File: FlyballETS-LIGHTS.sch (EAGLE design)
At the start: 21 parts, among them IC1 74HC595N, IC2 ULN2003AN, IC3 LM555N

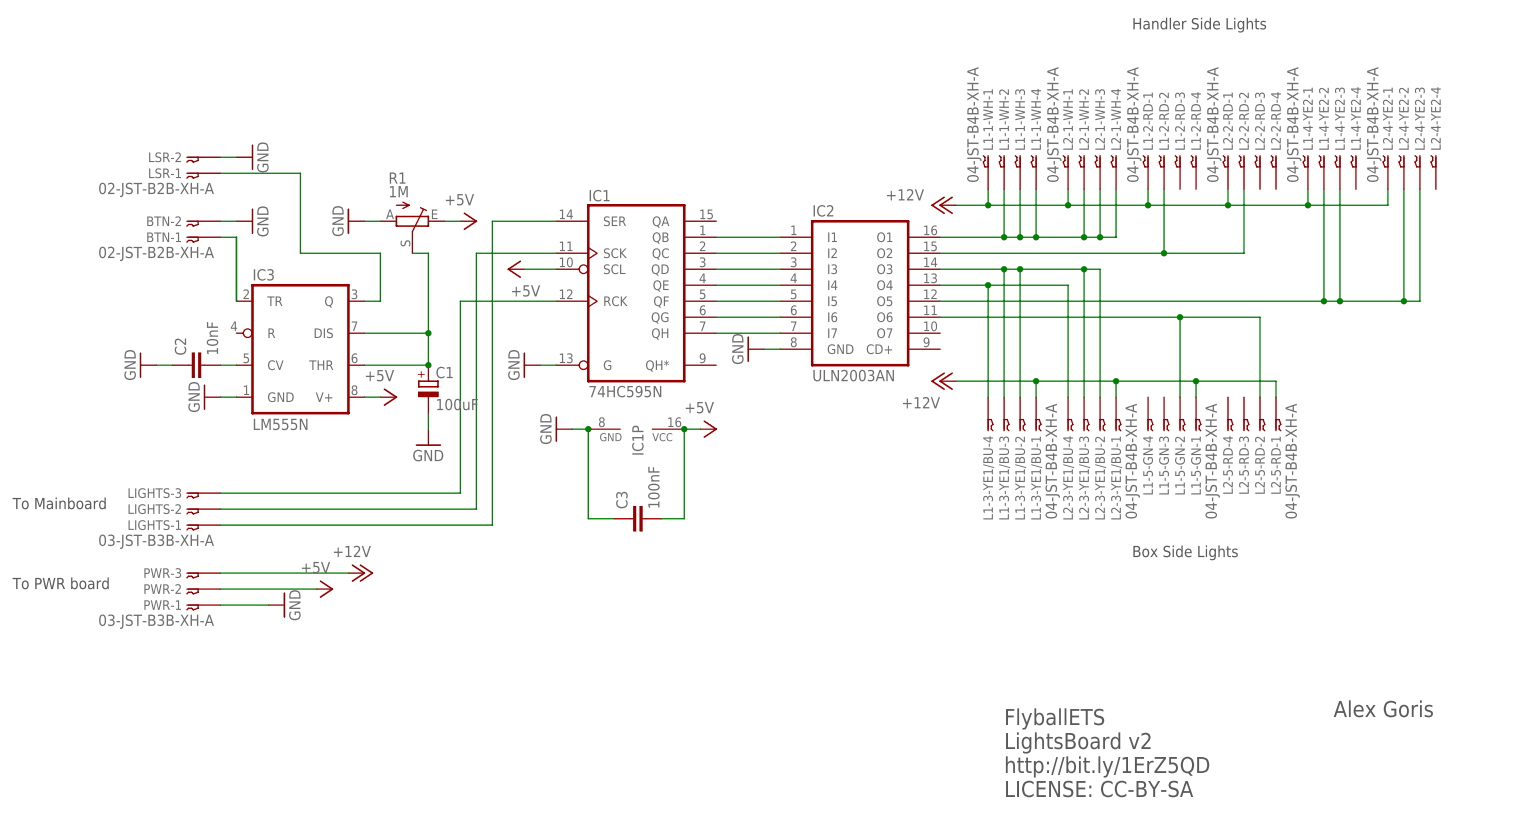
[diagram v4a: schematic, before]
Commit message: Fixed JST XH pin numbering
Updated bt_con-jst-xh.lbr library with swapped pin numbering.
Updated all board designs with updated library so they have the
connectors the right way around
Fixes #4
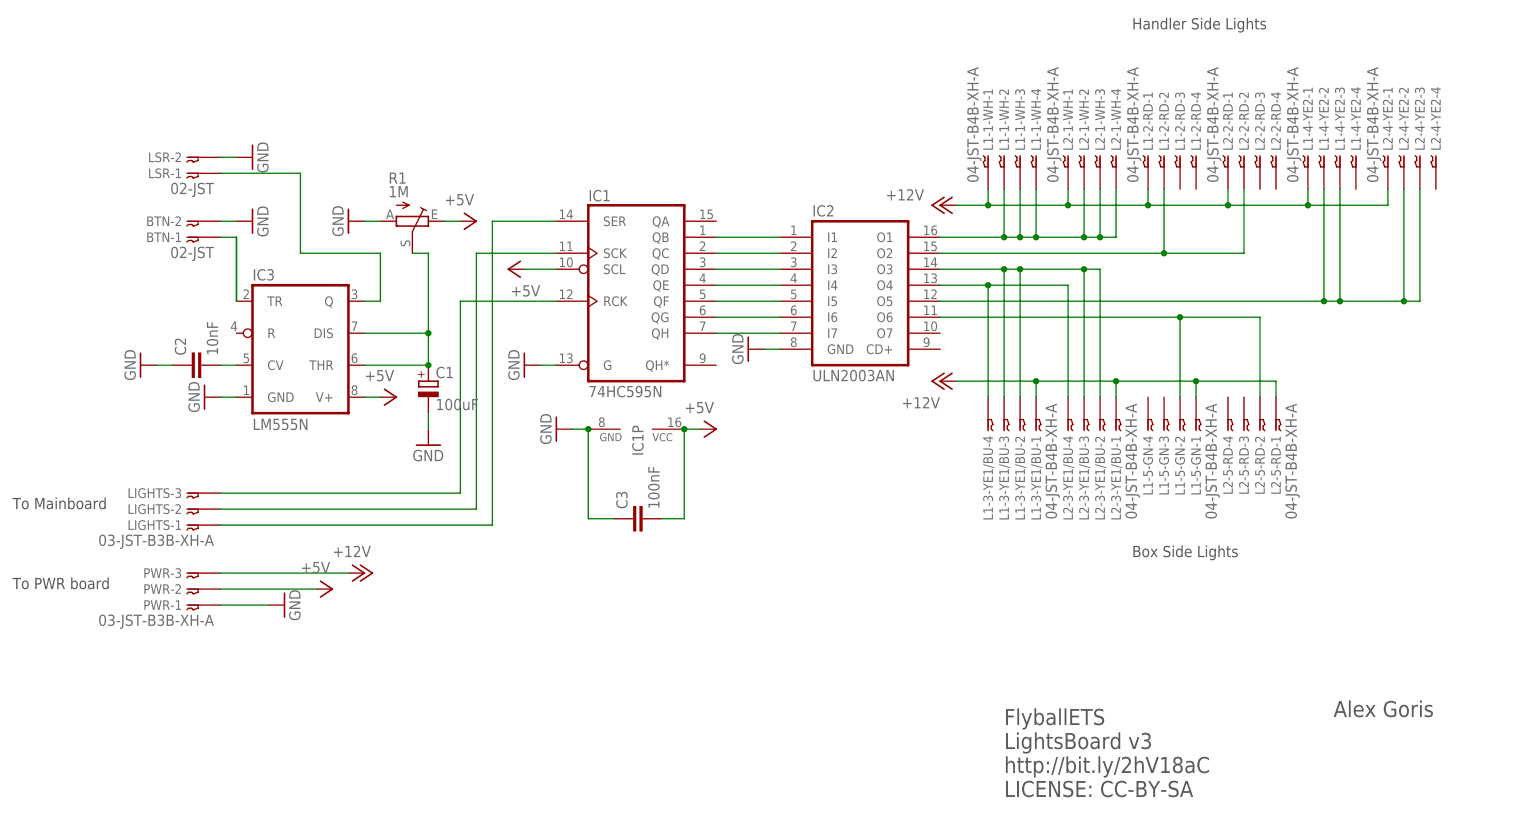
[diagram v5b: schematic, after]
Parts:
- BTN, LSR: value 02-JST-B2B-XH-A -> 02-JST; device bt_con-jst-xh:02-JST-B2B-XH-A -> bt_con-jst-xh:02-JST
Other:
- note added: "FlyballETS LightsBoard v3 http://bit.ly/2hV18aC LICENSE: CC-BY-SA"
- note removed: "FlyballETS LightsBoard v2 http://bit.ly/1ErZ5QD LICENSE: CC-BY-SA"
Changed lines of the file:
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@@
 <?xml version="1.0" encoding="utf-8"?>
 <!DOCTYPE eagle SYSTEM "eagle.dtd">
-<eagle version="7.5.0">
+<eagle version="8.2.2">
 <drawing>
 <settings>
@@
 </classes>
 <parts>
-<part name="BTN" library="bt_con-jst-xh" deviceset="02-JST" device="-B2B-XH-A"/>
-<part name="IC1" library="74xx-eu" deviceset="74*595" device="N" technology="HC"/>
-<part name="IC2" library="uln-udn" deviceset="ULN2003A" device="N"/>
-<part name="IC3" library="linear" deviceset="*555" device="N" technology="LM"/>
-<part name="R1" library="pot" deviceset="TRIM_EU-" device="B25P" value="1M"/>
-<part name="C1" library="resistor" deviceset="CPOL-EU" device="E2.5-7" value="100uF"/>
+<part name="BTN" library="bt_con-jst-xh" deviceset="02-JST" device=""/>
+<part name="IC1" library="74xx-eu" library_urn="urn:adsk.eagle:library:85" deviceset="74*595" device="N" technology="HC"/>
+<part name="IC2" library="uln-udn" library_urn="urn:adsk.eagle:library:407" deviceset="ULN2003A" device="N"/>
+<part name="IC3" library="linear" library_urn="urn:adsk.eagle:library:262" deviceset="*555" device="N" technology="LM"/>
+<part name="R1" library="pot" library_urn="urn:adsk.eagle:library:331" deviceset="TRIM_EU-" device="B25P" value="1M"/>
+<part name="C1" library="resistor" library_urn="urn:adsk.eagle:library:348" deviceset="CPOL-EU" device="E2.5-7" value="100uF"/>
 <part name="PWR" library="bt_con-jst-xh" deviceset="03-JST" device="-B3B-XH-A"/>
-<part name="GND1" library="supply1" deviceset="GND" device=""/>
-<part name="P+1" library="supply1" deviceset="+5V" device=""/>
-<part name="P+2" library="supply1" deviceset="+12V" device=""/>
+<part name="GND1" library="supply1" library_urn="urn:adsk.eagle:library:371" deviceset="GND" device=""/>
+<part name="P+1" library="supply1" library_urn="urn:adsk.eagle:library:371" deviceset="+5V" device=""/>
+<part name="P+2" library="supply1" library_urn="urn:adsk.eagle:library:371" deviceset="+12V" device=""/>
 <part name="LIGHTS" library="bt_con-jst-xh" deviceset="03-JST" device="-B3B-XH-A"/>
-<part name="P+3" library="supply1" deviceset="+5V" device=""/>
-<part name="GND2" library="supply1" deviceset="GND" device=""/>
-<part name="GND3" library="supply1" deviceset="GND" device=""/>
-<part name="GND4" library="supply1" deviceset="GND" device=""/>
+<part name="P+3" library="supply1" library_urn="urn:adsk.eagle:library:371" deviceset="+5V" device=""/>
+<part name="GND2" library="supply1" library_urn="urn:adsk.eagle:library:371" deviceset="GND" device=""/>
+<part name="GND3" library="supply1" library_urn="urn:adsk.eagle:library:371" deviceset="GND" device=""/>
+<part name="GND4" library="supply1" library_urn="urn:adsk.eagle:library:371" deviceset="GND" device=""/>
 <part name="L2-5-RD" library="bt_con-jst-xh" deviceset="04-JST" device="-B4B-XH-A"/>
 <part name="L2-4-YE2" library="bt_con-jst-xh" deviceset="04-JST" device="-B4B-XH-A"/>
@@
 <part name="L1-4-YE2" library="bt_con-jst-xh" deviceset="04-JST" device="-B4B-XH-A"/>
 <part name="L1-5-GN" library="bt_con-jst-xh" deviceset="04-JST" device="-B4B-XH-A"/>
-<part name="P+4" library="supply1" deviceset="+12V" device=""/>
-<part name="P+9" library="supply1" deviceset="+5V" device=""/>
-<part name="GND5" library="supply1" deviceset="GND" device=""/>
-<part name="P+10" library="supply1" deviceset="+5V" device=""/>
-<part name="GND6" library="supply1" deviceset="GND" device=""/>
-<part name="GND7" library="supply1" deviceset="GND" device=""/>
-<part name="C2" library="resistor" deviceset="C-EU" device="050-030X075" value="10nF"/>
-<part name="GND8" library="supply1" deviceset="GND" device=""/>
-<part name="GND9" library="supply1" deviceset="GND" device=""/>
-<part name="LSR" library="bt_con-jst-xh" deviceset="02-JST" device="-B2B-XH-A"/>
-<part name="GND10" library="supply1" deviceset="GND" device=""/>
-<part name="FRAME1" library="frames" deviceset="A4L-LOC" device=""/>
-<part name="P+7" library="supply1" deviceset="+12V" device=""/>
-<part name="C3" library="resistor" deviceset="C-EU" device="050-030X075" value="100nF"/>
-<part name="P+5" library="supply1" deviceset="+5V" device=""/>
+<part name="P+4" library="supply1" library_urn="urn:adsk.eagle:library:371" deviceset="+12V" device=""/>
+<part name="P+9" library="supply1" library_urn="urn:adsk.eagle:library:371" deviceset="+5V" device=""/>
+<part name="GND5" library="supply1" library_urn="urn:adsk.eagle:library:371" deviceset="GND" device=""/>
+<part name="P+10" library="supply1" library_urn="urn:adsk.eagle:library:371" deviceset="+5V" device=""/>
+<part name="GND6" library="supply1" library_urn="urn:adsk.eagle:library:371" deviceset="GND" device=""/>
+<part name="GND7" library="supply1" library_urn="urn:adsk.eagle:library:371" deviceset="GND" device=""/>
+<part name="C2" library="resistor" library_urn="urn:adsk.eagle:library:348" deviceset="C-EU" device="050-030X075" value="10nF"/>
+<part name="GND8" library="supply1" library_urn="urn:adsk.eagle:library:371" deviceset="GND" device=""/>
+<part name="GND9" library="supply1" library_urn="urn:adsk.eagle:library:371" deviceset="GND" device=""/>
+<part name="LSR" library="bt_con-jst-xh" deviceset="02-JST" device=""/>
+<part name="GND10" library="supply1" library_urn="urn:adsk.eagle:library:371" deviceset="GND" device=""/>
+<part name="FRAME1" library="frames" library_urn="urn:adsk.eagle:library:229" deviceset="A4L-LOC" device=""/>
+<part name="P+7" library="supply1" library_urn="urn:adsk.eagle:library:371" deviceset="+12V" device=""/>
+<part name="C3" library="resistor" library_urn="urn:adsk.eagle:library:348" deviceset="C-EU" device="050-030X075" value="100nF"/>
+<part name="P+5" library="supply1" library_urn="urn:adsk.eagle:library:371" deviceset="+5V" device=""/>
 </parts>
 <sheets>
@@
 <text x="160.02" y="12.7" size="1.778" layer="97">Box Side Lights</text>
 <text x="139.7" y="-25.4" size="2.54" layer="97">FlyballETS
-LightsBoard v2
-http://bit.ly/1ErZ5QD
+LightsBoard v3
+http://bit.ly/2hV18aC
 LICENSE: CC-BY-SA</text>
 <text x="192.024" y="-12.7" size="2.54" layer="97">Alex Goris</text>
@@
 which will not be processed correctly with this version.
 </note>
+<note version="8.2" severity="warning">
+Since Version 8.2, Eagle supports online libraries. The ids
+of those online libraries will not be understood (or retained)
+with this version.
+</note>
 </compatibility>
